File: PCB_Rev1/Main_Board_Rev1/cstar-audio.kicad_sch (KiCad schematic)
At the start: 0 parts

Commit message: Updated Audio Schematic
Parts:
- added J12, J13: 532610771, CSTAR-MainBoard-Footprints:MOLEX_532610771, symbol 532610771:532610771
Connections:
- new net +3V3: J12.3, J13.3
- new net GND: J12.2, J12.S1 (SHIELD1), J12.S2 (SHIELD2), J13.2, J13.S1 (SHIELD1), J13.S2 (SHIELD2)
- new net GPIO22: J12.7, J13.7
- new net GPIO??: J12.4, J12.5, J12.6, J13.4, J13.5, J13.6
- no-connect marks 0 -> 2
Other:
- note added: "MIC 1 (Unidirectional - Delamination)"
- note added: "MIC 2 (Omnidirectional - Environment)"

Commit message: Added Footprints + Updated Layout for Audio Connectors
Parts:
- J12, J13: footprint CSTAR-MainBoard-Footprints:MOLEX_532610771 -> Connector_Molex:Molex_PicoBlade_53261-0771_1x07-1MP_P1.25mm_Horizontal
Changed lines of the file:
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@@
 			)
 		)
-		(property "Footprint" "CSTAR-MainBoard-Footprints:MOLEX_532610771"
+		(property "Footprint" "Connector_Molex:Molex_PicoBlade_53261-0771_1x07-1MP_P1.25mm_Horizontal"
 			(at 210.82 105.41 0)
 			(effects
@@
 			)
 		)
-		(property "Footprint" "CSTAR-MainBoard-Footprints:MOLEX_532610771"
+		(property "Footprint" "Connector_Molex:Molex_PicoBlade_53261-0771_1x07-1MP_P1.25mm_Horizontal"
 			(at 91.44 105.41 0)
 			(effects

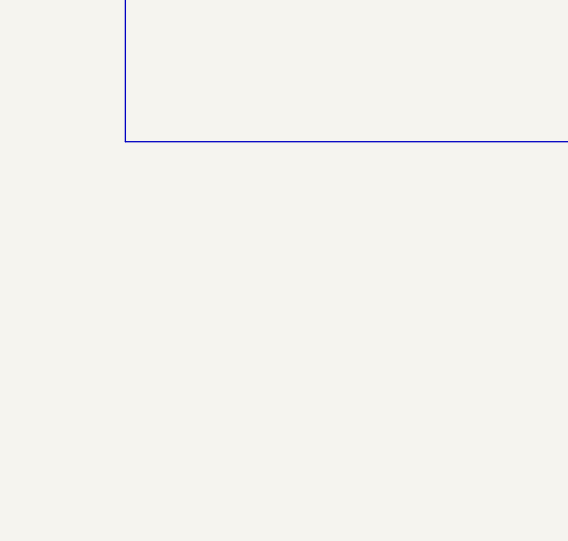
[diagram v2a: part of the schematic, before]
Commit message: Power nets updated in all schematics
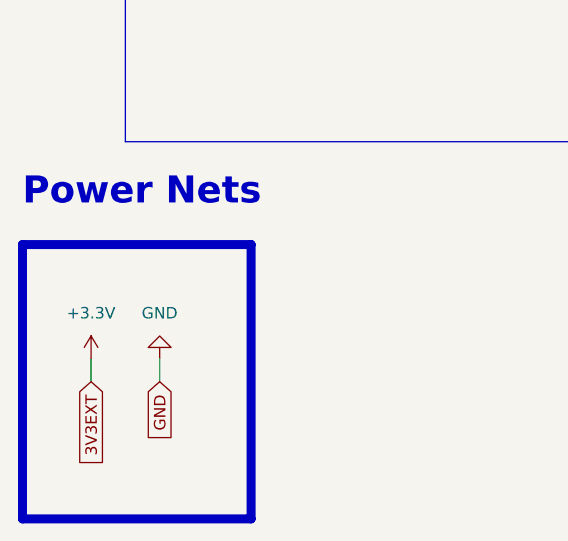
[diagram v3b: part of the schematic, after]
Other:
- note added: "Power Nets"
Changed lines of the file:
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@@
+	(wire
+		(pts
+			(xy 54.61 163.83) (xy 54.61 166.37)
+		)
+		(stroke
+			(width 0)
+			(type default)
+		)
+	)
 	(wire
 		(pts
@@
 		(pts
 			(xy 189.23 99.06) (xy 198.12 99.06)
+		)
+		(stroke
+			(width 0)
+			(type default)
+		)
+	)
+	(wire
+		(pts
+			(xy 46.99 163.83) (xy 46.99 166.37)
 		)
 		(stroke
@@
 		(stroke
 			(width 0)
+			(type default)
+		)
+		(fill
+			(type none)
+		)
+	)
+	(rectangle
+		(start 39.37 151.13)
+		(end 64.77 181.61)
+		(stroke
+			(width 1)
 			(type default)
 		)
@@
 		)
 	)
+	(text "Power Nets"
+		(exclude_from_sim no)
+		(at 39.37 147.066 0)
+		(effects
+			(font
+				(size 3 3)
+				(thickness 0.6)
+				(bold yes)
+			)
+			(justify left bottom)
+		)
+	)
 	(text "MIC 1 (Unidirectional - Delamination)"
 		(exclude_from_sim no)
@@
 		(property "Intersheetrefs" "${INTERSHEET_REFS}"
 			(at 68.3845 113.03 0)
+			(effects
+				(font
+					(size 1.27 1.27)
+				)
+				(justify right)
+				(hide yes)
+			)
+		)
+	)
+	(global_label "GND"
+		(shape input)
+		(at 54.61 166.37 270)
+		(fields_autoplaced yes)
+		(effects
+			(font
+				(size 1.27 1.27)
+			)
+			(justify right)
+		)
+		(property "Intersheetrefs" "${INTERSHEET_REFS}"
+			(at 54.61 173.2257 90)
+			(effects
+				(font
+					(size 1.27 1.27)
+				)
+				(justify right)
+				(hide yes)
+			)
+		)
+	)
+	(global_label "3V3EXT"
+		(shape input)
+		(at 46.99 166.37 270)
+		(fields_autoplaced yes)
+		(effects
+			(font
+				(size 1.27 1.27)
+			)
+			(justify right)
+		)
+		(property "Intersheetrefs" "${INTERSHEET_REFS}"
+			(at 46.99 176.1889 90)
 			(effects
 				(font
@@
 				(path "/8f5a23de-a1fa-4202-92fb-c2ac3de0338c/ddfb4fd8-d336-4db3-9d74-da06ae92f0f2"
 					(reference "J13")
+					(unit 1)
+				)
+			)
+		)
+	)
+	(symbol
+		(lib_id "power:GND")
+		(at 54.61 163.83 180)
+		(unit 1)
+		(exclude_from_sim no)
+		(in_bom yes)
+		(on_board yes)
+		(dnp no)
+		(fields_autoplaced yes)
+		(property "Reference" "#PWR063"
+			(at 54.61 157.48 0)
+			(effects
+				(font
+					(size 1.27 1.27)
+				)
+				(hide yes)
+			)
+		)
+		(property "Value" "GND"
+			(at 54.61 158.75 0)
+			(effects
+				(font
+					(size 1.27 1.27)
+				)
+			)
+		)
+		(property "Footprint" ""
+			(at 54.61 163.83 0)
+			(effects
+				(font
+					(size 1.27 1.27)
+				)
+				(hide yes)
+			)
+		)
+		(property "Datasheet" ""
+			(at 54.61 163.83 0)
+			(effects
+				(font
+					(size 1.27 1.27)
+				)
+				(hide yes)
+			)
+		)
+		(property "Description" "Power symbol creates a global label with name \"GND\" , ground"
+			(at 54.61 163.83 0)
+			(effects
+				(font
+					(size 1.27 1.27)
+				)
+				(hide yes)
+			)
+		)
+		(pin "1"
+		)
+		(instances
+			(project "Main_Board_Rev1"
+				(path "/8f5a23de-a1fa-4202-92fb-c2ac3de0338c/ddfb4fd8-d336-4db3-9d74-da06ae92f0f2"
+					(reference "#PWR063")
 					(unit 1)
 				)
@@
 					(unit 1)
 				)
+			)
+		)
+	)
+	(symbol
+		(lib_id "power:+3.3V")
+		(at 46.99 163.83 0)
+		(unit 1)
+		(exclude_from_sim no)
+		(in_bom yes)
+		(on_board yes)
+		(dnp no)
+		(fields_autoplaced yes)
+		(property "Reference" "#PWR062"
+			(at 46.99 167.64 0)
+			(effects
+				(font
+					(size 1.27 1.27)
+				)
+				(hide yes)
+			)
+		)
+		(property "Value" "+3.3V"
+			(at 46.99 158.75 0)
+			(effects
+				(font
+					(size 1.27 1.27)
+				)
+			)
+		)
+		(property "Footprint" ""
+			(at 46.99 163.83 0)
+			(effects
+				(font
+					(size 1.27 1.27)
+				)
+				(hide yes)
+			)
+		)
+		(property "Datasheet" ""
+			(at 46.99 163.83 0)
+			(effects
+				(font
+					(size 1.27 1.27)
+				)
+				(hide yes)
+			)
+		)
+		(property "Description" "Power symbol creates a global label with name \"+3.3V\""
+			(at 46.99 163.83 0)
+			(effects
+				(font
+					(size 1.27 1.27)
+				)
+				(hide yes)
+			)
+		)
+		(pin "1"
+		)
+		(instances
+			(project "Main_Board_Rev1"
+				(path "/8f5a23de-a1fa-4202-92fb-c2ac3de0338c/ddfb4fd8-d336-4db3-9d74-da06ae92f0f2"
+					(reference "#PWR062")
+					(unit 1)
+				)

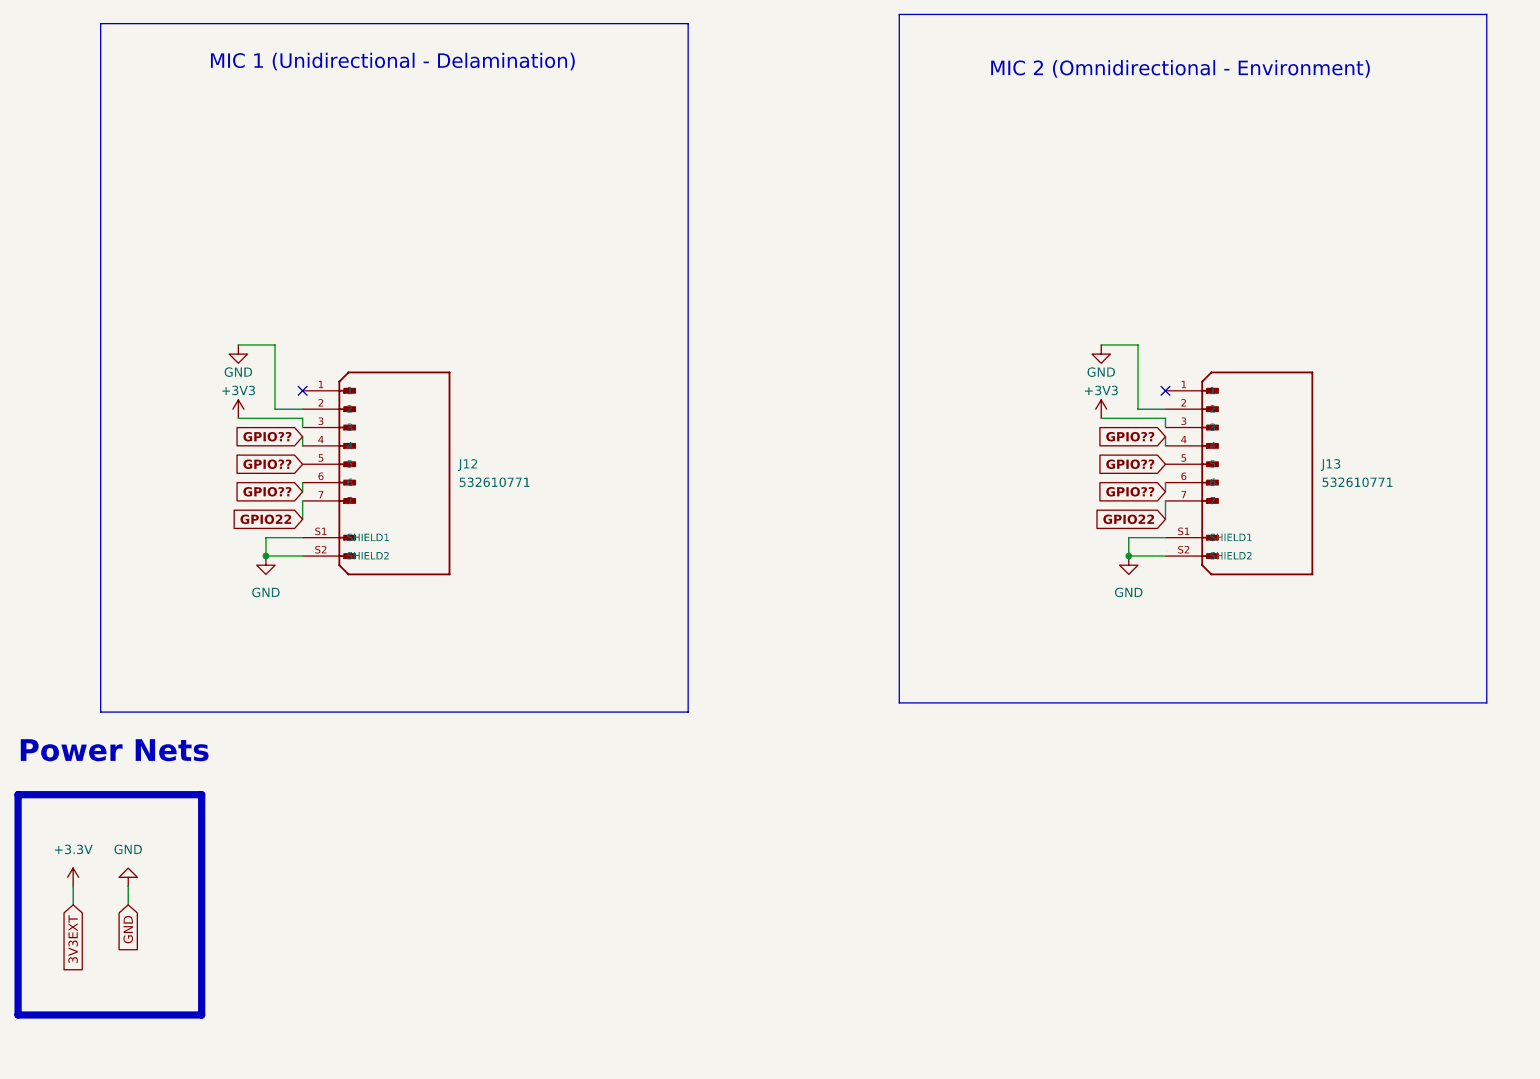
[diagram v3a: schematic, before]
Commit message: Connections to RPi GPIO Pins + Eliminating Errors from Layout
Global net connections made from RPi GPIO pins.
Error for mounting hole corrected -> mounting hole symbol imported into schematic and correct footprint assigned.
Warnings for J10, J11, J12 connectors resolved- imported footprint for the connector from online (error in the one imported from KiCAD libraries with pins S1 and S2 labeled as MP in the footprint)
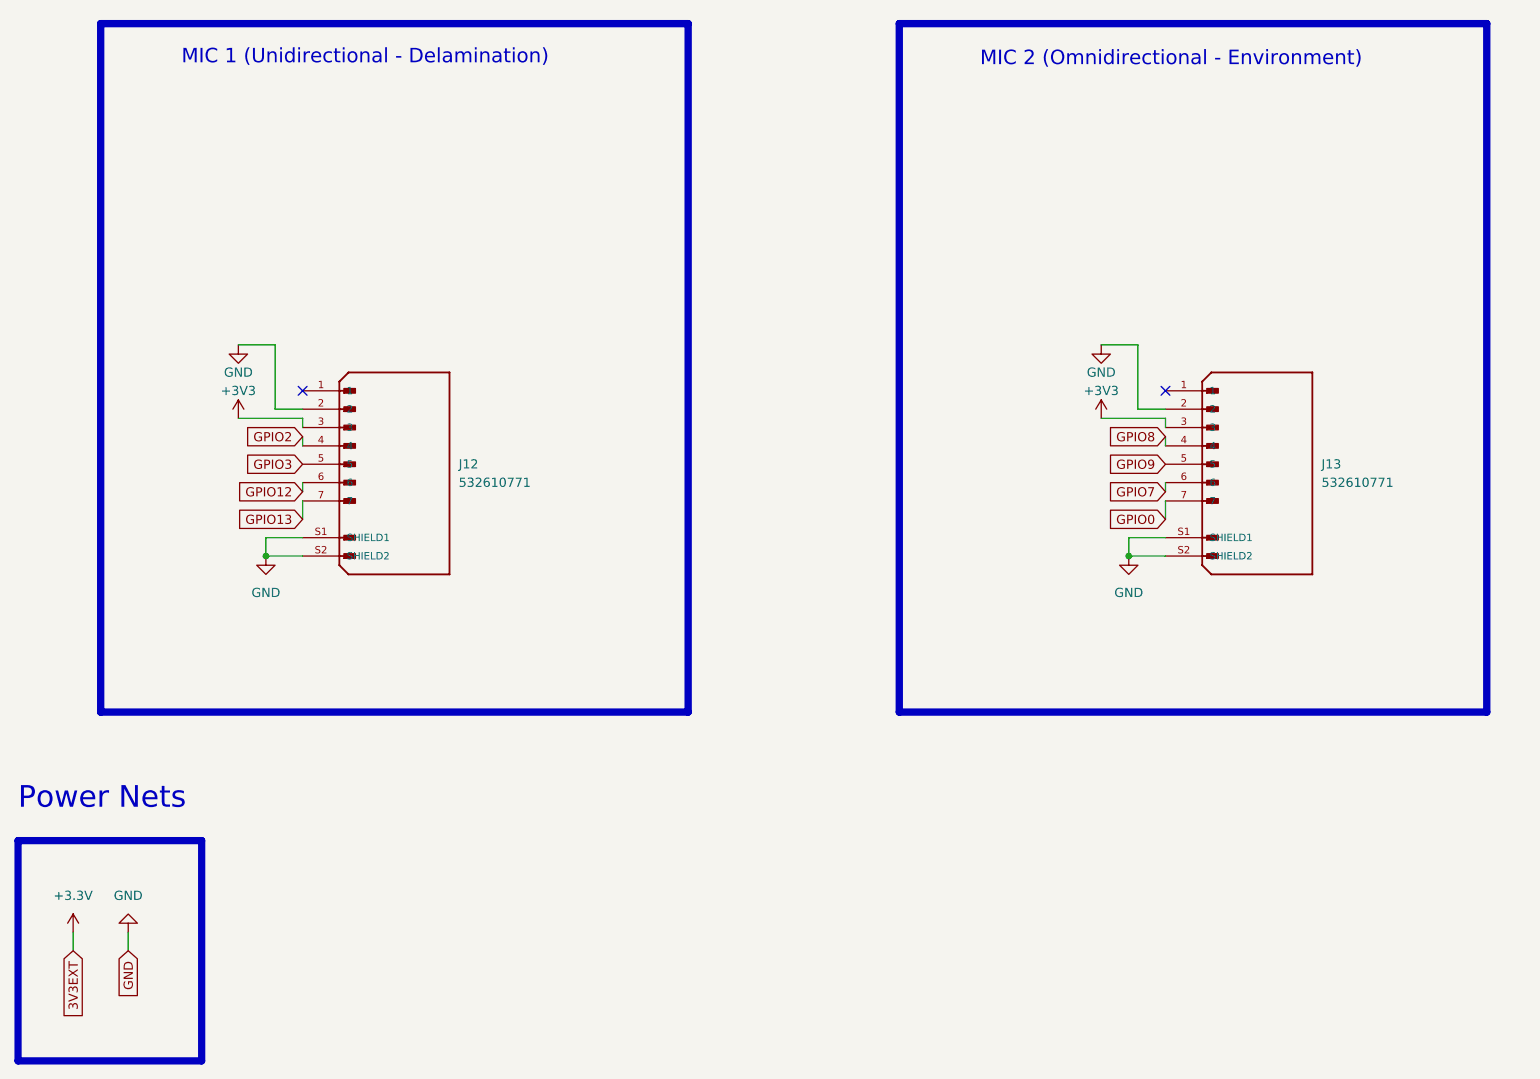
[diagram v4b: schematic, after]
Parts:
- J12, J13: footprint Connector_Molex:Molex_PicoBlade_53261-0771_1x07-1MP_P1.25mm_Horizontal -> Footprints:MOLEX_connector
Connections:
- net GPIO22 renamed GPIO0
- net GPIO0: no longer J12.7
- removed net GPIO??: J12.4, J12.5, J12.6, J13.4, J13.5, J13.6
- new net GPIO12: J12.6
- new net GPIO13: J12.7
- new net GPIO2: J12.4
- new net GPIO3: J12.5
- new net GPIO7: J13.6
- new net GPIO8: J13.4
- new net GPIO9: J13.5
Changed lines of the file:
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@@
 	(wire
 		(pts
-			(xy 54.61 163.83) (xy 54.61 166.37)
+			(xy 54.61 170.18) (xy 54.61 172.72)
 		)
 		(stroke
@@
 	(wire
 		(pts
-			(xy 46.99 163.83) (xy 46.99 166.37)
+			(xy 46.99 170.18) (xy 46.99 172.72)
 		)
 		(stroke
@@
 		(end 132.08 139.7)
 		(stroke
-			(width 0)
+			(width 1.016)
 			(type default)
 		)
@@
 	)
 	(rectangle
-		(start 39.37 151.13)
-		(end 64.77 181.61)
+		(start 39.37 157.48)
+		(end 64.77 187.96)
 		(stroke
 			(width 1)
@@
 	)
 	(rectangle
-		(start 161.29 43.18)
-		(end 242.57 138.43)
-		(stroke
-			(width 0)
+		(start 161.29 44.45)
+		(end 242.57 139.7)
+		(stroke
+			(width 1.016)
 			(type default)
 		)
@@
 	(text "MIC 2 (Omnidirectional - Environment)"
 		(exclude_from_sim no)
-		(at 173.736 52.07 0)
+		(at 172.466 50.546 0)
 		(effects
 			(font
 				(size 2 2)
+				(thickness 0.25)
 			)
 			(justify left bottom)
@@
 	(text "Power Nets"
 		(exclude_from_sim no)
-		(at 39.37 147.066 0)
+		(at 39.37 153.416 0)
 		(effects
 			(font
 				(size 3 3)
-				(thickness 0.6)
-				(bold yes)
+				(thickness 0.375)
 			)
 			(justify left bottom)
@@
 	(text "MIC 1 (Unidirectional - Delamination)"
 		(exclude_from_sim no)
-		(at 65.786 51.054 0)
+		(at 61.976 50.292 0)
 		(effects
 			(font
 				(size 2 2)
+				(thickness 0.25)
 			)
 			(justify left bottom)
 		)
 	)
-	(global_label "GPIO22"
+	(global_label "GPIO13"
 		(shape input)
 		(at 78.74 113.03 180)
@@
 			(font
 				(size 1.27 1.27)
-				(bold yes)
+				(thickness 0.1588)
 			)
 			(justify right)
@@
 	(global_label "GND"
 		(shape input)
-		(at 54.61 166.37 270)
+		(at 54.61 172.72 270)
 		(fields_autoplaced yes)
 		(effects
@@
 		)
 		(property "Intersheetrefs" "${INTERSHEET_REFS}"
-			(at 54.61 173.2257 90)
+			(at 54.61 179.5757 90)
 			(effects
 				(font
@@
 	(global_label "3V3EXT"
 		(shape input)
-		(at 46.99 166.37 270)
+		(at 46.99 172.72 270)
 		(fields_autoplaced yes)
 		(effects
@@
 		)
 		(property "Intersheetrefs" "${INTERSHEET_REFS}"
-			(at 46.99 176.1889 90)
+			(at 46.99 182.5389 90)
 			(effects
 				(font
@@
 		)
 	)
-	(global_label "GPIO??"
+	(global_label "GPIO7"
 		(shape input)
 		(at 198.12 109.22 180)
@@
 			(font
 				(size 1.27 1.27)
-				(bold yes)
+				(thickness 0.1588)
 			)
 			(justify right)
 		)
 		(property "Intersheetrefs" "${INTERSHEET_REFS}"
-			(at 188.0063 109.22 0)
+			(at 188.974 109.22 0)
 			(effects
 				(font
@@
 		)
 	)
-	(global_label "GPIO??"
+	(global_label "GPIO3"
 		(shape input)
 		(at 78.74 105.41 180)
@@
 			(font
 				(size 1.27 1.27)
-				(bold yes)
+				(thickness 0.1588)
 			)
 			(justify right)
 		)
 		(property "Intersheetrefs" "${INTERSHEET_REFS}"
-			(at 68.6263 105.41 0)
+			(at 69.594 105.41 0)
 			(effects
 				(font
@@
 		)
 	)
-	(global_label "GPIO22"
+	(global_label "GPIO0"
 		(shape input)
 		(at 198.12 113.03 180)
@@
 			(font
 				(size 1.27 1.27)
-				(bold yes)
+				(thickness 0.1588)
 			)
 			(justify right)
 		)
 		(property "Intersheetrefs" "${INTERSHEET_REFS}"
-			(at 187.7645 113.03 0)
+			(at 188.974 113.03 0)
 			(effects
 				(font
@@
 		)
 	)
-	(global_label "GPIO??"
+	(global_label "GPIO2"
 		(shape input)
 		(at 78.74 101.6 180)
@@
 			(font
 				(size 1.27 1.27)
-				(bold yes)
+				(thickness 0.1588)
 			)
 			(justify right)
 		)
 		(property "Intersheetrefs" "${INTERSHEET_REFS}"
-			(at 68.6263 101.6 0)
+			(at 69.594 101.6 0)
 			(effects
 				(font
@@
 		)
 	)
-	(global_label "GPIO??"
+	(global_label "GPIO9"
 		(shape input)
 		(at 198.12 105.41 180)
@@
 			(font
 				(size 1.27 1.27)
-				(bold yes)
+				(thickness 0.1588)
 			)
 			(justify right)
 		)
 		(property "Intersheetrefs" "${INTERSHEET_REFS}"
-			(at 188.0063 105.41 0)
+			(at 188.974 105.41 0)
 			(effects
 				(font
@@
 		)
 	)
-	(global_label "GPIO??"
+	(global_label "GPIO12"
 		(shape input)
 		(at 78.74 109.22 180)
@@
 			(font
 				(size 1.27 1.27)
-				(bold yes)
+				(thickness 0.1588)
 			)
 			(justify right)
 		)
 		(property "Intersheetrefs" "${INTERSHEET_REFS}"
-			(at 68.6263 109.22 0)
+			(at 68.3845 109.22 0)
 			(effects
 				(font
@@
 		)
 	)
-	(global_label "GPIO??"
+	(global_label "GPIO8"
 		(shape input)
 		(at 198.12 101.6 180)
@@
 			(font
 				(size 1.27 1.27)
-				(bold yes)
+				(thickness 0.1588)
 			)
 			(justify right)
 		)
 		(property "Intersheetrefs" "${INTERSHEET_REFS}"
-			(at 188.0063 101.6 0)
+			(at 188.974 101.6 0)
 			(effects
 				(font
@@
 			)
 		)
-		(property "Footprint" "Connector_Molex:Molex_PicoBlade_53261-0771_1x07-1MP_P1.25mm_Horizontal"
+		(property "Footprint" "Footprints:MOLEX_connector"
 			(at 210.82 105.41 0)
 			(effects
@@
 	(symbol
 		(lib_id "power:GND")
-		(at 54.61 163.83 180)
+		(at 54.61 170.18 180)
 		(unit 1)
 		(exclude_from_sim no)
@@
 		(fields_autoplaced yes)
 		(property "Reference" "#PWR063"
-			(at 54.61 157.48 0)
+			(at 54.61 163.83 0)
 			(effects
 				(font
@@
 		)
 		(property "Value" "GND"
-			(at 54.61 158.75 0)
+			(at 54.61 165.1 0)
 			(effects
 				(font
@@
 		)
 		(property "Footprint" ""
-			(at 54.61 163.83 0)
+			(at 54.61 170.18 0)
 			(effects
 				(font
@@
 		)
 		(property "Datasheet" ""
-			(at 54.61 163.83 0)
+			(at 54.61 170.18 0)
 			(effects
 				(font
@@
 		)
 		(property "Description" "Power symbol creates a global label with name \"GND\" , ground"
-			(at 54.61 163.83 0)
+			(at 54.61 170.18 0)
 			(effects
 				(font
@@
 			)
 		)
-		(property "Footprint" "Connector_Molex:Molex_PicoBlade_53261-0771_1x07-1MP_P1.25mm_Horizontal"
+		(property "Footprint" "Footprints:MOLEX_connector"
 			(at 91.44 105.41 0)
 			(effects
@@
 	(symbol
 		(lib_id "power:+3.3V")
-		(at 46.99 163.83 0)
+		(at 46.99 170.18 0)
 		(unit 1)
 		(exclude_from_sim no)
@@
 		(fields_autoplaced yes)
 		(property "Reference" "#PWR062"
-			(at 46.99 167.64 0)
+			(at 46.99 173.99 0)
 			(effects
 				(font
@@
 		)
 		(property "Value" "+3.3V"
-			(at 46.99 158.75 0)
+			(at 46.99 165.1 0)
 			(effects
 				(font
@@
 		)
 		(property "Footprint" ""
-			(at 46.99 163.83 0)
+			(at 46.99 170.18 0)
 			(effects
 				(font
@@
 		)
 		(property "Datasheet" ""
-			(at 46.99 163.83 0)
+			(at 46.99 170.18 0)
 			(effects
 				(font
@@
 		)
 		(property "Description" "Power symbol creates a global label with name \"+3.3V\""
-			(at 46.99 163.83 0)
-			(effects
-				(font
+			(at 46.99 170.18 0)
+			(effects
+				(font
